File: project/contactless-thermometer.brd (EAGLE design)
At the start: 50 x 150 mm, 92 parts, among them J1 OLED, J2 ICSP, J3 BLE, J4 USB-MINIB-5PIN, Q1 MMBT3904, Q2 MMBT3904, Q3 ZXMP6A17GTA, U1 LT1167CS8#PBF, U2 OPA2705UA, U3 OPA705NA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

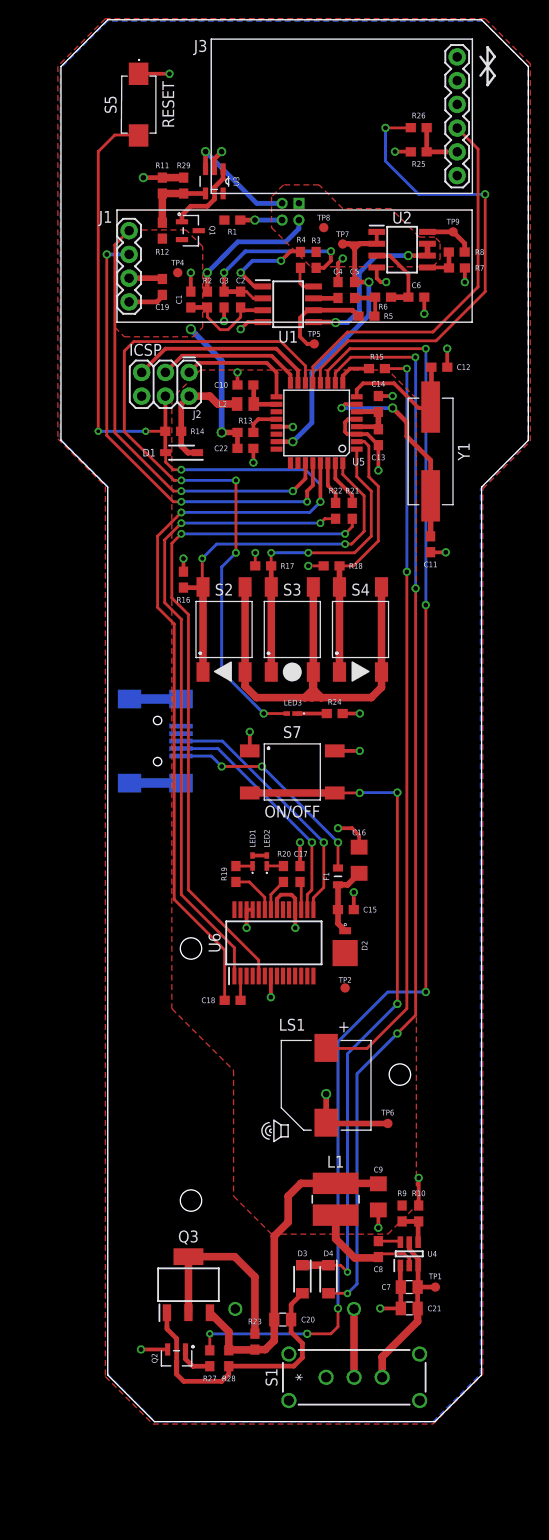
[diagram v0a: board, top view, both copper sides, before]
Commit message: update silkscreen and schematic
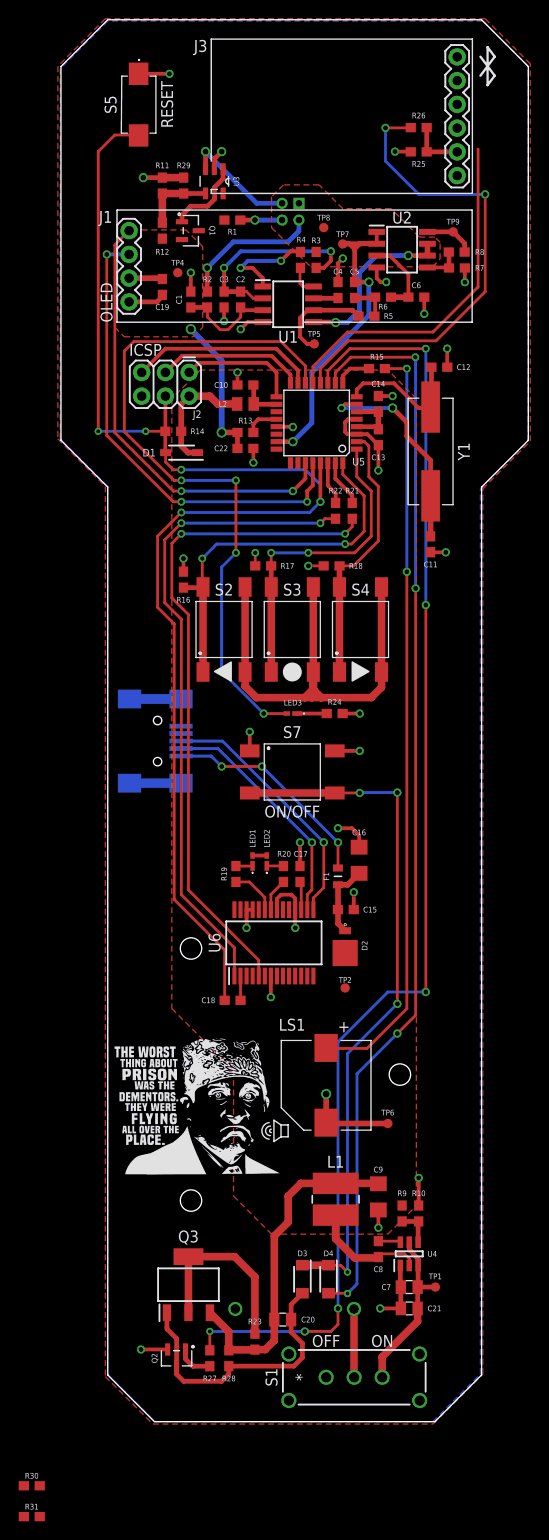
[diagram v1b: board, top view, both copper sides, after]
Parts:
- added R30: 1K, SparkFun-Resistors:0603
- added R31: 2K, SparkFun-Resistors:0603
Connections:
- removed net N$4: R1.1, TH1.3
- new net N$36: J3.4, R30.1, R31.2
- new net VR: R1.1, TH1.3, U5.24
- net BLE_RX: now also R30.2; no longer J3.4
- net GND: now also R31.1
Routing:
- net VR: track 0.00 -> 4.47 mm, vias 0 -> 1
- net N$4: track 4.47 -> 0.00 mm, vias 1 -> 0
- net BLE_RX: track 40.9 -> 37.7 mm
- net N$2: track 10.4 -> 10.9 mm
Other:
- board text added: "OFF"
- board text added: "OLED"
- board text added: "ON"

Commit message: snake
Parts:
- moved R31 160.1 mm to (33.3, 144.5)
- moved R30 154.3 mm to (33.3, 141.7), turned to 180 degrees
- moved TP8 3.59 mm to (26.7, 127.3)
- moved R26 0.25 mm to (33.3, 138.7)
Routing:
- net VR: track 4.47 -> 60.4 mm, vias 1 -> 3
- net BLE_RX: track 37.7 -> 52.6 mm, vias 0 -> 2
- net N$36: track 0.00 -> 7.93 mm
- net GND: track 115.2 -> 117.0 mm, vias 35 -> 36
- net TX: track 71.0 -> 71.6 mm

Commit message: Major Updates
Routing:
- net N$45: track 74.5 -> 73.4 mm
- net PWR_OUT: track 139.5 -> 138.9 mm
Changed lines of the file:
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@@
 <wire x1="29.6536" y1="112.6744" x2="32.004" y2="112.6744" width="0.3048" layer="1"/>
 <wire x1="23.368" y1="39.9918" x2="23.4249" y2="39.9349" width="0.3048" layer="1"/>
-<wire x1="32.004" y1="90.932" x2="32.004" y2="44.196" width="0.3048" layer="1"/>
+<wire x1="32.004" y1="90.932" x2="32.004" y2="44.45" width="0.3048" layer="1"/>
 <via x="32.004" y="112.6744" extent="1-16" drill="0.45"/>
 <via x="32.004" y="90.932" extent="1-16" drill="0.5"/>
 <wire x1="32.004" y1="112.6744" x2="32.004" y2="90.932" width="0.3048" layer="16"/>
-<wire x1="32.004" y1="44.196" x2="27.7429" y2="39.9349" width="0.3048" layer="1"/>
-<wire x1="27.7429" y1="39.9349" x2="23.4249" y2="39.9349" width="0.3048" layer="1"/>
+<wire x1="32.004" y1="44.45" x2="27.4889" y2="39.9349" width="0.3048" layer="1"/>
+<wire x1="27.4889" y1="39.9349" x2="23.4249" y2="39.9349" width="0.3048" layer="1"/>
 </signal>
 <signal name="BUT_R">
@@
 <via x="34.036" y="87.376" extent="1-16" drill="0.5"/>
 <via x="34.036" y="45.974" extent="1-16" drill="0.5"/>
-<wire x1="34.036" y1="45.974" x2="29.972" y2="45.974" width="0.3048" layer="16"/>
+<wire x1="34.036" y1="45.974" x2="30.988" y2="45.974" width="0.3048" layer="16"/>
 <wire x1="21.082" y1="9.652" x2="10.922" y2="9.652" width="0.3048" layer="16"/>
-<wire x1="29.972" y1="45.974" x2="24.638" y2="40.64" width="0.3048" layer="16"/>
-<wire x1="24.638" y1="40.64" x2="24.638" y2="12.1158" width="0.3048" layer="16"/>
+<wire x1="30.988" y1="45.974" x2="24.638" y2="39.624" width="0.3048" layer="16"/>
+<wire x1="24.638" y1="39.624" x2="24.638" y2="12.1158" width="0.3048" layer="16"/>
 <via x="21.082" y="9.652" extent="1-16" drill="0.5"/>
-<wire x1="24.638" y1="10.414" x2="23.876" y2="9.652" width="0.3048" layer="1"/>
-<wire x1="21.082" y1="9.652" x2="23.876" y2="9.652" width="0.3048" layer="1"/>
-<wire x1="24.638" y1="12.1158" x2="24.638" y2="10.414" width="0.3048" layer="1"/>
+<wire x1="21.7678" y1="12.1158" x2="21.082" y2="11.43" width="0.3048" layer="1"/>
+<wire x1="21.082" y1="9.652" x2="21.082" y2="11.43" width="0.3048" layer="1"/>
+<wire x1="24.638" y1="12.1158" x2="21.7678" y2="12.1158" width="0.3048" layer="1"/>
 <via x="24.638" y="12.1158" extent="1-16" drill="0.5"/>
 </signal>
@@
 <wire x1="15.196" y1="67.2698" x2="24.296" y2="67.2698" width="0.8128" layer="1"/>
 <wire x1="23.622" y1="16.74" x2="20.828" y2="16.74" width="0.8128" layer="1"/>
-<via x="25.654" y="16.002" extent="1-16" drill="0.4"/>
 <wire x1="24.296" y1="67.2698" x2="26.9642" y2="67.2698" width="0.3048" layer="1"/>
-<wire x1="23.622" y1="16.74" x2="24.916" y2="16.74" width="0.3048" layer="1"/>
-<wire x1="24.916" y1="16.74" x2="25.654" y2="16.002" width="0.3048" layer="1"/>
 <via x="30.988" y="44.704" extent="1-16" drill="0.5"/>
-<wire x1="25.654" y1="39.37644375" x2="25.654" y2="16.002" width="0.3048" layer="16"/>
+<wire x1="25.6286" y1="39.35104375" x2="25.6286" y2="16.7386" width="0.3048" layer="16"/>
 <wire x1="30.988" y1="44.704" x2="30.98155625" y2="44.704" width="0.3048" layer="16"/>
-<wire x1="30.98155625" y1="44.704" x2="25.654" y2="39.37644375" width="0.3048" layer="16"/>
+<wire x1="30.98155625" y1="44.704" x2="25.6286" y2="39.35104375" width="0.3048" layer="16"/>
 <wire x1="30.988" y1="67.31" x2="30.988" y2="44.704" width="0.3048" layer="1"/>
 <via x="30.988" y="67.31" extent="1-16" drill="0.5"/>
@@
 <wire x1="26.9642" y1="67.2698" x2="27.0044" y2="67.31" width="0.3048" layer="16"/>
 <via x="26.9642" y="67.2698" extent="1-16" drill="0.5"/>
+<via x="25.6286" y="16.7386" extent="1-16" drill="0.45"/>
+<wire x1="25.6286" y1="16.7386" x2="23.6234" y2="16.7386" width="0.4064" layer="1"/>
+<wire x1="23.6234" y1="16.7386" x2="23.622" y2="16.74" width="0.4064" layer="1"/>
 </signal>
 <signal name="PWR_IN">
@@
 <wire x1="32.9438" y1="113.8682" x2="32.9438" y2="89.154" width="0.3048" layer="16"/>
 <via x="32.9438" y="89.154" extent="1-16" drill="0.5"/>
-<wire x1="32.9438" y1="43.4868" x2="30.988" y2="41.531" width="0.3048" layer="1"/>
-<via x="30.988" y="41.531" extent="1-16" drill="0.5"/>
-<wire x1="32.9438" y1="89.154" x2="32.9438" y2="43.4868" width="0.3048" layer="1"/>
-<wire x1="26.67" y1="14.732" x2="25.654" y2="13.716" width="0.3048" layer="16"/>
-<wire x1="30.988" y1="41.531" x2="26.67" y2="37.213" width="0.3048" layer="16"/>
-<wire x1="26.67" y1="37.213" x2="26.67" y2="14.732" width="0.3048" layer="16"/>
+<wire x1="32.9438" y1="44.2488" x2="30.226" y2="41.531" width="0.3048" layer="1"/>
+<via x="30.226" y="41.531" extent="1-16" drill="0.5"/>
+<wire x1="32.9438" y1="89.154" x2="32.9438" y2="44.2488" width="0.3048" layer="1"/>
+<wire x1="26.416" y1="16.256" x2="25.654" y2="15.494" width="0.3048" layer="16"/>
+<wire x1="25.654" y1="15.494" x2="25.654" y2="13.716" width="0.3048" layer="16"/>
+<wire x1="30.226" y1="41.531" x2="26.416" y2="37.721" width="0.3048" layer="16"/>
+<wire x1="26.416" y1="37.721" x2="26.416" y2="16.256" width="0.3048" layer="16"/>
 </signal>
 <signal name="N$2">
